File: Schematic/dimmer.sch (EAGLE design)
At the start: 18 parts, among them Q1 IRF840, T1 BC547

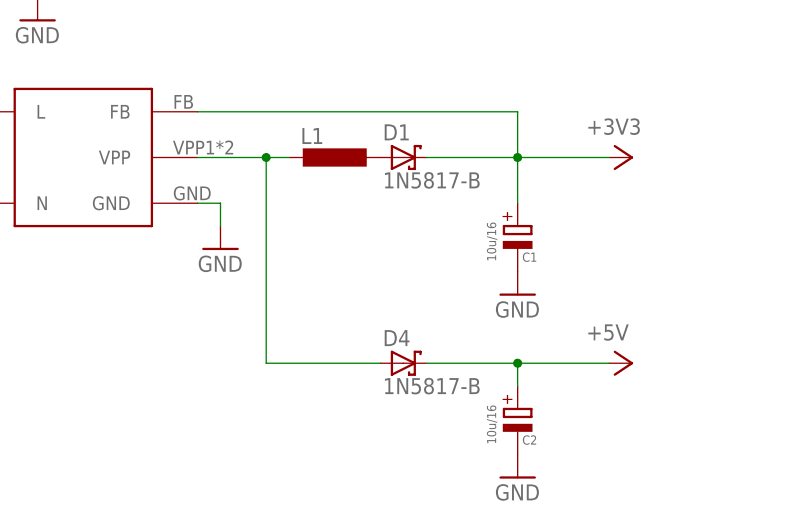
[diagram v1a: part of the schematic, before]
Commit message: Add L dimension
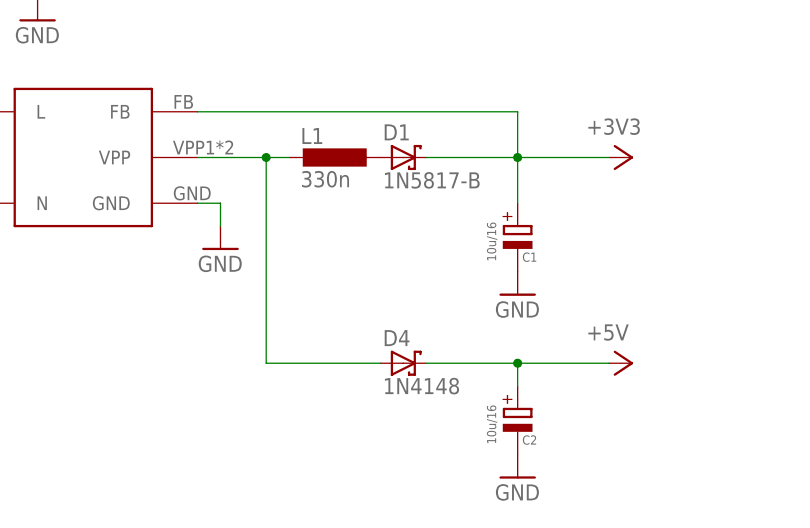
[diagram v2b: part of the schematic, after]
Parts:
- D4: value 1N5817-B -> 1N4148
- L1: value (none) -> 330n
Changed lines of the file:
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@@
 <part name="GND7" library="supply1" deviceset="GND" device=""/>
 <part name="GND9" library="supply1" deviceset="GND" device=""/>
-<part name="L1" library="rcl" deviceset="L-EU" device="0204/5"/>
+<part name="L1" library="rcl" deviceset="L-EU" device="0204/5" value="330n"/>
 <part name="P+1" library="supply1" deviceset="+5V" device=""/>
 <part name="U$1" library="esp8266modules" deviceset="ESP8266" device=""/>
@@
 <part name="GND6" library="supply1" deviceset="GND" device=""/>
 <part name="D1" library="diode" deviceset="1N581*" device="" technology="7-B"/>
-<part name="D4" library="diode" deviceset="1N581*" device="" technology="7-B"/>
+<part name="D4" library="diode" deviceset="1N581*" device="" technology="7-B" value="1N4148"/>
 <part name="F3" library="fuse" deviceset="FUSE" device="SHK20L" value="1A flink"/>
 <part name="U$2" library="smps" deviceset="SMPS" device=""/>
